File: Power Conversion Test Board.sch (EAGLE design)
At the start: 39 parts, among them U1 LM2678, U2 LM2678

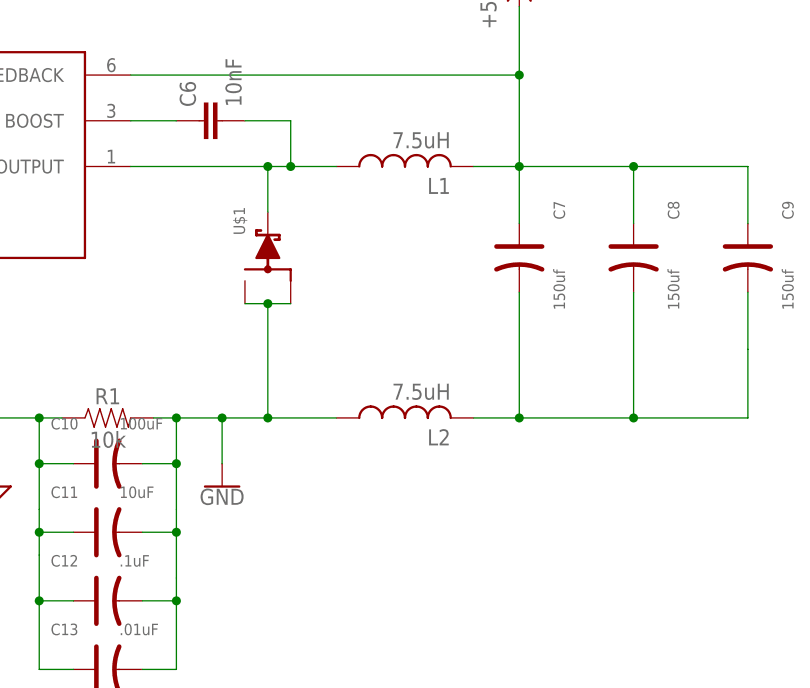
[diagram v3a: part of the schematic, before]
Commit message: Added components to allow fixing if it doesnt work with split inductors, @melchor repeat with the 12->5v3 circuit
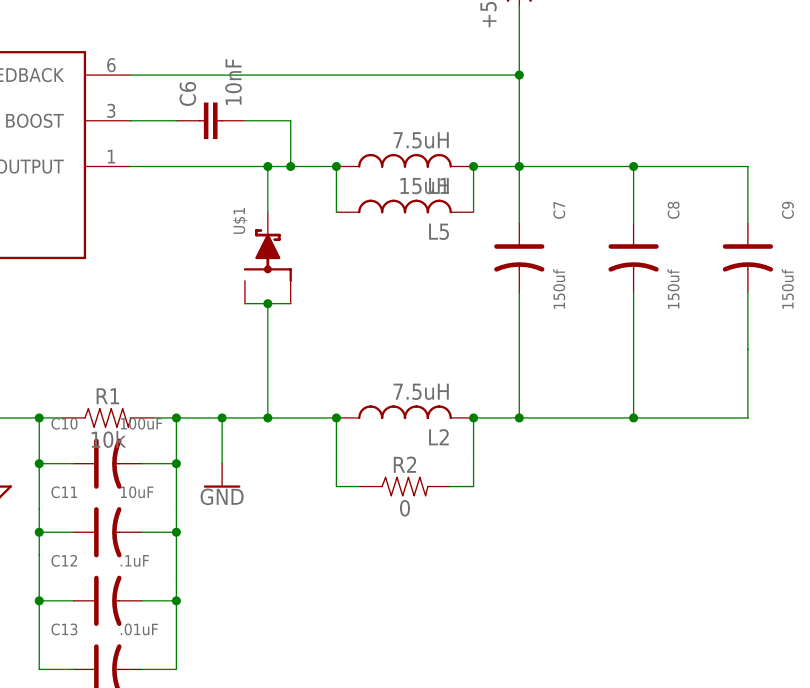
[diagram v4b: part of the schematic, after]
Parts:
- added L5: 15uH, rcl:L-USL2012C
- added R2: 0, SparkFun-Resistors:RESISTOR0603
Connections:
- net +5V: now also L5.2
- net GND_5V: now also R2.1
- net N$1: now also L5.1
- net N$8: now also R2.2
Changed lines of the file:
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@@
 <part name="GND5" library="SparkFun-PowerSymbols" library_urn="urn:adsk.eagle:library:530" deviceset="GND" device=""/>
 <part name="U$2" library="microbuilder" deviceset="GND" device=""/>
+<part name="R2" library="SparkFun-Resistors" library_urn="urn:adsk.eagle:library:532" deviceset="RESISTOR" device="0603" package3d_urn="urn:adsk.eagle:package:39650/1" value="0"/>
+<part name="L5" library="rcl" library_urn="urn:adsk.eagle:library:334" deviceset="L-US" device="L2012C" package3d_urn="urn:adsk.eagle:package:23475/1" value="15uH"/>
 </parts>
 <sheets>
@@
 <instance part="GND5" gate="1" x="182.88" y="106.68"/>
 <instance part="U$2" gate="G$1" x="401.32" y="106.68"/>
+<instance part="R2" gate="G$1" x="203.2" y="106.68"/>
+<instance part="L5" gate="G$1" x="203.2" y="137.16" rot="R90">
+<attribute name="NAME" x="208.28" y="135.89" size="1.778" layer="95" rot="R180"/>
+<attribute name="VALUE" x="208.28" y="140.97" size="1.778" layer="96" rot="R180"/>
+</instance>
 </instances>
 <busses>
@@
 <pinref part="C9" gate="G$1" pin="-"/>
 <wire x1="241.3" y1="121.92" x2="241.3" y2="128.27" width="0.1524" layer="91"/>
+<wire x1="210.82" y1="114.3" x2="210.82" y2="109.22" width="0.1524" layer="91"/>
+<junction x="210.82" y="114.3"/>
+<pinref part="R2" gate="G$1" pin="2"/>
+<wire x1="208.28" y1="106.68" x2="210.82" y2="106.68" width="0.1524" layer="91"/>
+<wire x1="210.82" y1="106.68" x2="210.82" y2="109.22" width="0.1524" layer="91"/>
 </segment>
 </net>
@@
 <wire x1="172.72" y1="152.4" x2="215.9" y2="152.4" width="0.1524" layer="91"/>
 <junction x="215.9" y="152.4"/>
+<pinref part="L5" gate="G$1" pin="2"/>
+<wire x1="210.82" y1="142.24" x2="210.82" y2="137.16" width="0.1524" layer="91"/>
+<junction x="210.82" y="142.24"/>
 </segment>
 </net>
@@
 <wire x1="187.96" y1="137.16" x2="187.96" y2="142.24" width="0.1524" layer="91"/>
 <junction x="187.96" y="142.24"/>
+<wire x1="195.58" y1="142.24" x2="195.58" y2="139.7" width="0.1524" layer="91"/>
+<junction x="195.58" y="142.24"/>
+<wire x1="195.58" y1="139.7" x2="195.58" y2="137.16" width="0.1524" layer="91"/>
+<pinref part="L5" gate="G$1" pin="1"/>
 </segment>
 </net>
@@
 <junction x="182.88" y="114.3"/>
 <pinref part="GND5" gate="1" pin="GND"/>
-</segment>
-</net>
+<wire x1="195.58" y1="114.3" x2="195.58" y2="109.22" width="0.1524" layer="91"/>
+<junction x="195.58" y="114.3"/>
+<pinref part="R2" gate="G$1" pin="1"/>
+<wire x1="198.12" y1="106.68" x2="195.58" y2="106.68" width="0.1524" layer="91"/>
+<wire x1="195.58" y1="106.68" x2="195.58" y2="109.22" width="0.1524" layer="91"/>
+</segment>
+</net>

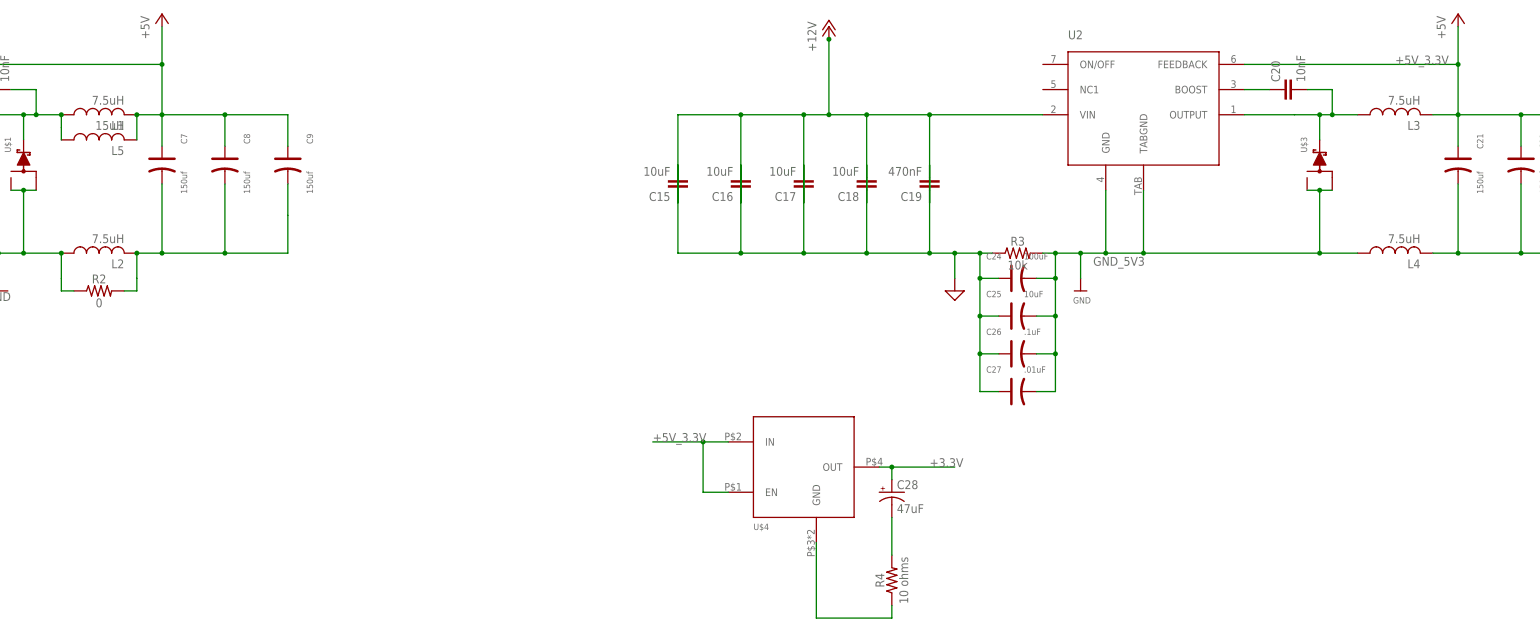
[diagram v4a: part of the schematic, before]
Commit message: Fixed Resistor Value
Fixed the resistor value on the 3.3 V linear regulator line
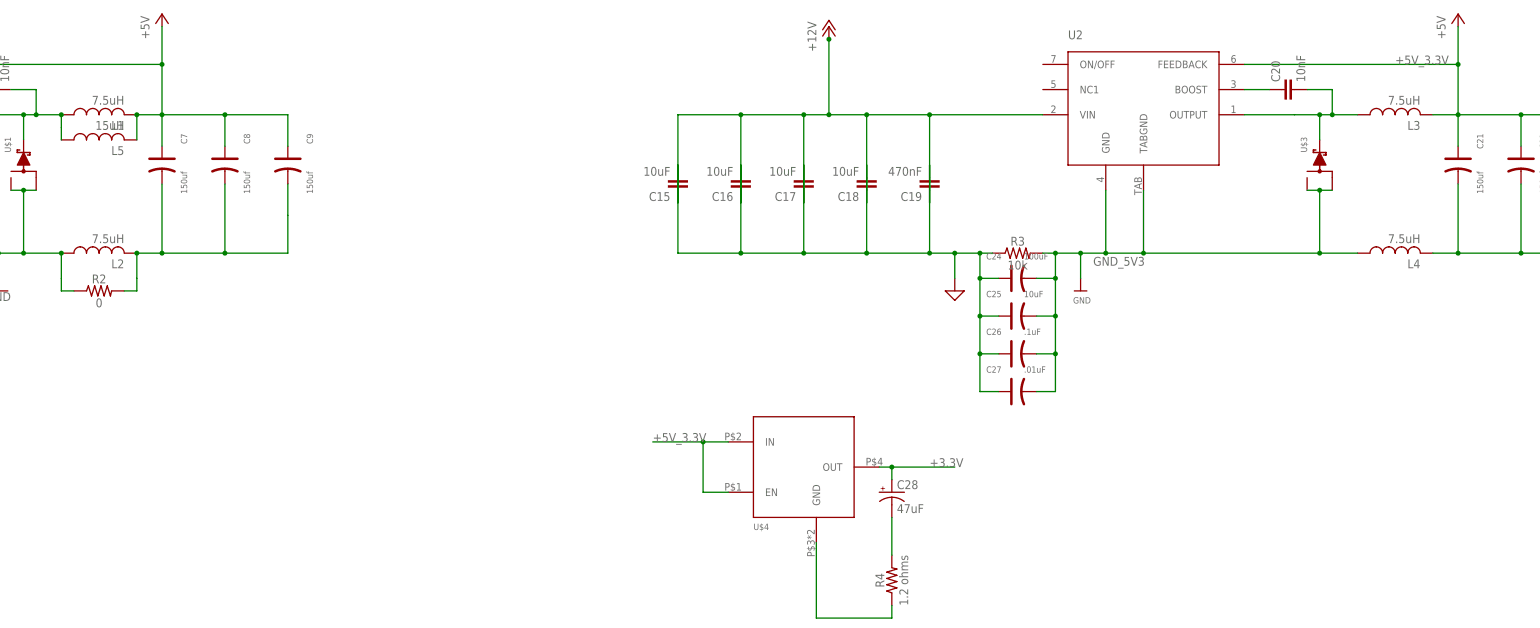
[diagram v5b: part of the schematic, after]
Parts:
- R4: value 10 ohms -> 1.2 ohms
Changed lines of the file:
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@@
 <?xml version="1.0" encoding="utf-8"?>
 <!DOCTYPE eagle SYSTEM "eagle.dtd">
-<eagle version="9.1.3">
+<eagle version="9.2.0">
 <drawing>
 <settings>
@@
 <part name="U$4" library="TPS758" deviceset="TO-263" device=""/>
 <part name="C28" library="SparkFun-Capacitors" library_urn="urn:adsk.eagle:library:510" deviceset="47UF-POLAR" device="-EIA3528-10V-10%" package3d_urn="urn:adsk.eagle:package:37411/1" value="47uF"/>
-<part name="R4" library="SparkFun-Resistors" library_urn="urn:adsk.eagle:library:532" deviceset="RESISTOR" device="0603" package3d_urn="urn:adsk.eagle:package:39650/1" value=" 10 ohms"/>
+<part name="R4" library="SparkFun-Resistors" library_urn="urn:adsk.eagle:library:532" deviceset="RESISTOR" device="0603" package3d_urn="urn:adsk.eagle:package:39650/1" value=" 1.2 ohms"/>
 <part name="GND5" library="SparkFun-PowerSymbols" library_urn="urn:adsk.eagle:library:530" deviceset="GND" device=""/>
 <part name="U$2" library="microbuilder" deviceset="GND" device=""/>
@@
 <attribute name="VALUE" x="469.9" y="118.11" size="1.778" layer="96" rot="R180"/>
 </instance>
-<instance part="P+3" gate="1" x="477.52" y="162.56"/>
+<instance part="P+3" gate="1" x="477.52" y="162.56">
+<attribute name="VALUE" x="474.98" y="157.48" size="1.778" layer="96" rot="R90"/>
+</instance>
 <instance part="P+4" gate="1" x="350.52" y="160.02">
 <attribute name="VALUE" x="347.98" y="154.94" size="1.778" layer="96" rot="R90"/>
@@
 <attribute name="VALUE" x="364.744" y="48.26" size="1.778" layer="96" font="vector" rot="R90" align="top-center"/>
 </instance>
-<instance part="GND5" gate="1" x="182.88" y="106.68"/>
-<instance part="U$2" gate="G$1" x="401.32" y="106.68"/>
-<instance part="R2" gate="G$1" x="203.2" y="106.68"/>
+<instance part="GND5" gate="1" x="182.88" y="106.68">
+<attribute name="VALUE" x="182.88" y="106.426" size="1.778" layer="96" align="top-center"/>
+</instance>
+<instance part="U$2" gate="G$1" x="401.32" y="106.68">
+<attribute name="VALUE" x="399.796" y="104.14" size="1.27" layer="96"/>
+</instance>
+<instance part="R2" gate="G$1" x="203.2" y="106.68">
+<attribute name="NAME" x="203.2" y="108.204" size="1.778" layer="95" font="vector" align="bottom-center"/>
+<attribute name="VALUE" x="203.2" y="105.156" size="1.778" layer="96" font="vector" align="top-center"/>
+</instance>
 <instance part="L5" gate="G$1" x="203.2" y="137.16" rot="R90">
 <attribute name="NAME" x="208.28" y="135.89" size="1.778" layer="95" rot="R180"/>

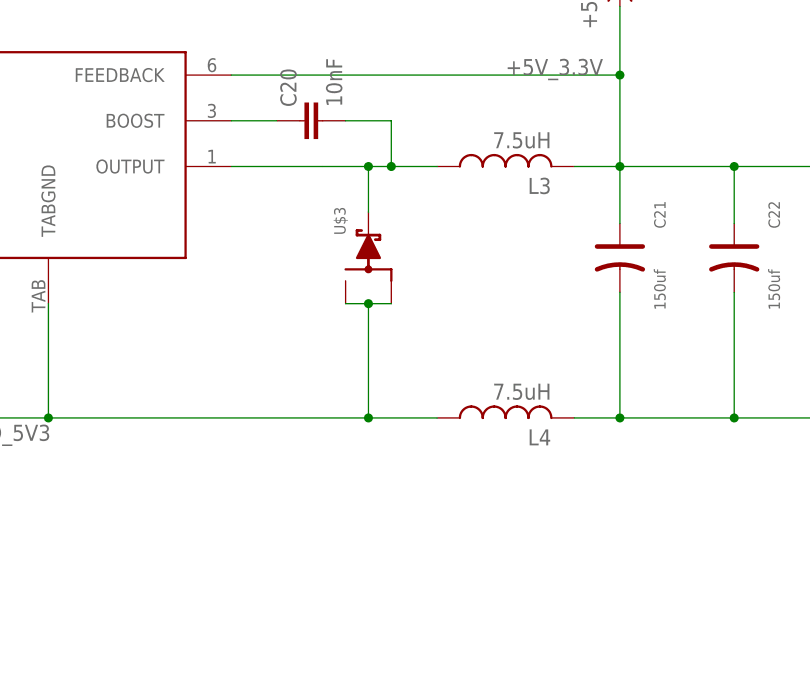
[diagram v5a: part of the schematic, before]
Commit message: added the resistor and inductor
added the 0ohm resistor and 15 uH inductor to the other buck
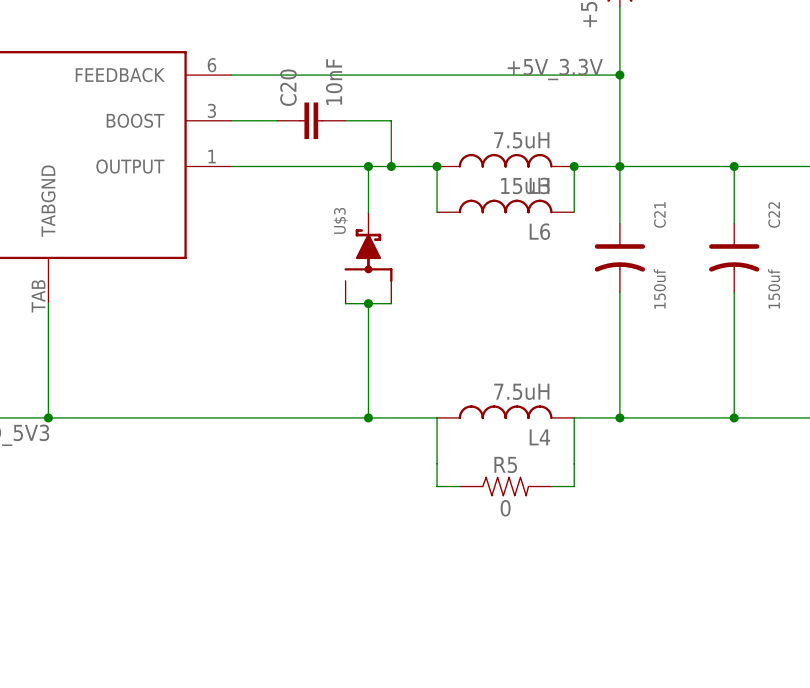
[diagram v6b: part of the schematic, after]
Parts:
- added L6: 15uH, rcl:L-USL2012C
- added R5: 0, SparkFun-Resistors:RESISTOR0603
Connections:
- new net GND_5V1: R5.1
- new net N$4: R5.2
- net +5V_3.3V: now also L6.2
- net N$7: now also L6.1
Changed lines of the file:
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@@
 <part name="R2" library="SparkFun-Resistors" library_urn="urn:adsk.eagle:library:532" deviceset="RESISTOR" device="0603" package3d_urn="urn:adsk.eagle:package:39650/1" value="0"/>
 <part name="L5" library="rcl" library_urn="urn:adsk.eagle:library:334" deviceset="L-US" device="L2012C" package3d_urn="urn:adsk.eagle:package:23475/1" value="15uH"/>
+<part name="L6" library="rcl" library_urn="urn:adsk.eagle:library:334" deviceset="L-US" device="L2012C" package3d_urn="urn:adsk.eagle:package:23475/1" value="15uH"/>
+<part name="R5" library="SparkFun-Resistors" library_urn="urn:adsk.eagle:library:532" deviceset="RESISTOR" device="0603" package3d_urn="urn:adsk.eagle:package:39650/1" value="0"/>
 </parts>
 <sheets>
@@
 <attribute name="NAME" x="208.28" y="135.89" size="1.778" layer="95" rot="R180"/>
 <attribute name="VALUE" x="208.28" y="140.97" size="1.778" layer="96" rot="R180"/>
+</instance>
+<instance part="L6" gate="G$1" x="464.82" y="137.16" rot="R90">
+<attribute name="NAME" x="469.9" y="135.89" size="1.778" layer="95" rot="R180"/>
+<attribute name="VALUE" x="469.9" y="140.97" size="1.778" layer="96" rot="R180"/>
+</instance>
+<instance part="R5" gate="G$1" x="464.82" y="106.68">
+<attribute name="NAME" x="464.82" y="108.204" size="1.778" layer="95" font="vector" align="bottom-center"/>
+<attribute name="VALUE" x="464.82" y="105.156" size="1.778" layer="96" font="vector" align="top-center"/>
 </instance>
 </instances>
@@
 <segment>
 <pinref part="U2" gate="G$1" pin="OUTPUT"/>
-<wire x1="434.34" y1="142.24" x2="444.5" y2="142.24" width="0.1524" layer="91"/>
+<wire x1="434.34" y1="142.24" x2="449.58" y2="142.24" width="0.1524" layer="91"/>
 <pinref part="C20" gate="G$1" pin="2"/>
 <wire x1="447.04" y1="147.32" x2="452.12" y2="147.32" width="0.1524" layer="91"/>
@@
 <pinref part="L3" gate="G$1" pin="1"/>
 <wire x1="457.2" y1="142.24" x2="452.12" y2="142.24" width="0.1524" layer="91"/>
-<wire x1="444.5" y1="142.24" x2="449.58" y2="142.24" width="0.1524" layer="91"/>
 <junction x="452.12" y="142.24"/>
 <pinref part="U$3" gate="G$1" pin="P$4"/>
@@
 <wire x1="449.58" y1="137.16" x2="449.58" y2="142.24" width="0.1524" layer="91"/>
 <junction x="449.58" y="142.24"/>
+<pinref part="L6" gate="G$1" pin="1"/>
+<wire x1="457.2" y1="142.24" x2="457.2" y2="137.16" width="0.1524" layer="91"/>
+<junction x="457.2" y="142.24"/>
 </segment>
 </net>
@@
 <junction x="477.52" y="152.4"/>
 <label x="464.82" y="152.4" size="1.778" layer="95"/>
+<pinref part="L6" gate="G$1" pin="2"/>
+<wire x1="472.44" y1="137.16" x2="472.44" y2="142.24" width="0.1524" layer="91"/>
+<junction x="472.44" y="142.24"/>
 </segment>
 <segment>
@@
 </segment>
 </net>
+<net name="N$4" class="0">
+<segment>
+<wire x1="472.44" y1="114.3" x2="472.44" y2="109.22" width="0.1524" layer="91"/>
+<pinref part="R5" gate="G$1" pin="2"/>
+<wire x1="469.9" y1="106.68" x2="472.44" y2="106.68" width="0.1524" layer="91"/>
+<wire x1="472.44" y1="106.68" x2="472.44" y2="109.22" width="0.1524" layer="91"/>
+</segment>
+</net>
+<net name="GND_5V1" class="0">
+<segment>
+<wire x1="457.2" y1="114.3" x2="457.2" y2="109.22" width="0.1524" layer="91"/>
+<pinref part="R5" gate="G$1" pin="1"/>
+<wire x1="459.74" y1="106.68" x2="457.2" y2="106.68" width="0.1524" layer="91"/>
+<wire x1="457.2" y1="106.68" x2="457.2" y2="109.22" width="0.1524" layer="91"/>
+</segment>
+</net>

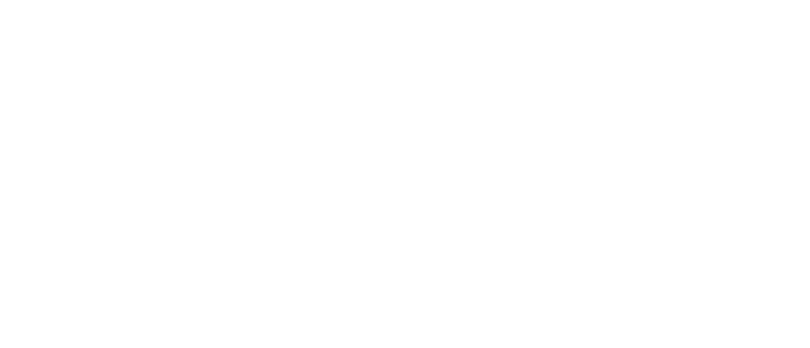
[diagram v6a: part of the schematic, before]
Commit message: added the outline
should go according to this outline, but dont need to for the test board
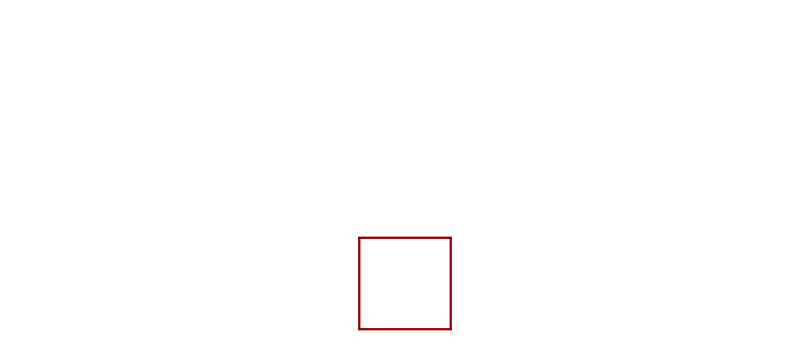
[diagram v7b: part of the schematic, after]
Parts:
- added U$5: BOARDPCB, board_outlines:BOARDPCB
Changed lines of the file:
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@@
 <part name="L6" library="rcl" library_urn="urn:adsk.eagle:library:334" deviceset="L-US" device="L2012C" package3d_urn="urn:adsk.eagle:package:23475/1" value="15uH"/>
 <part name="R5" library="SparkFun-Resistors" library_urn="urn:adsk.eagle:library:532" deviceset="RESISTOR" device="0603" package3d_urn="urn:adsk.eagle:package:39650/1" value="0"/>
+<part name="U$5" library="board_outlines" deviceset="BOARD" device="PCB"/>
 </parts>
 <sheets>
@@
 <attribute name="VALUE" x="464.82" y="105.156" size="1.778" layer="96" font="vector" align="top-center"/>
 </instance>
+<instance part="U$5" gate="G$1" x="243.84" y="40.64"/>
 </instances>
 <busses>
